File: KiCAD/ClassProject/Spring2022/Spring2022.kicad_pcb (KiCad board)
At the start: 2 copper layers, 211 x 39 mm, 40 parts, among them U1 FUB-MINI, U2 74HC595, U3 74HC595, U4 74HC595, U5 74HC595, U6 74HC595, U7 74HC595

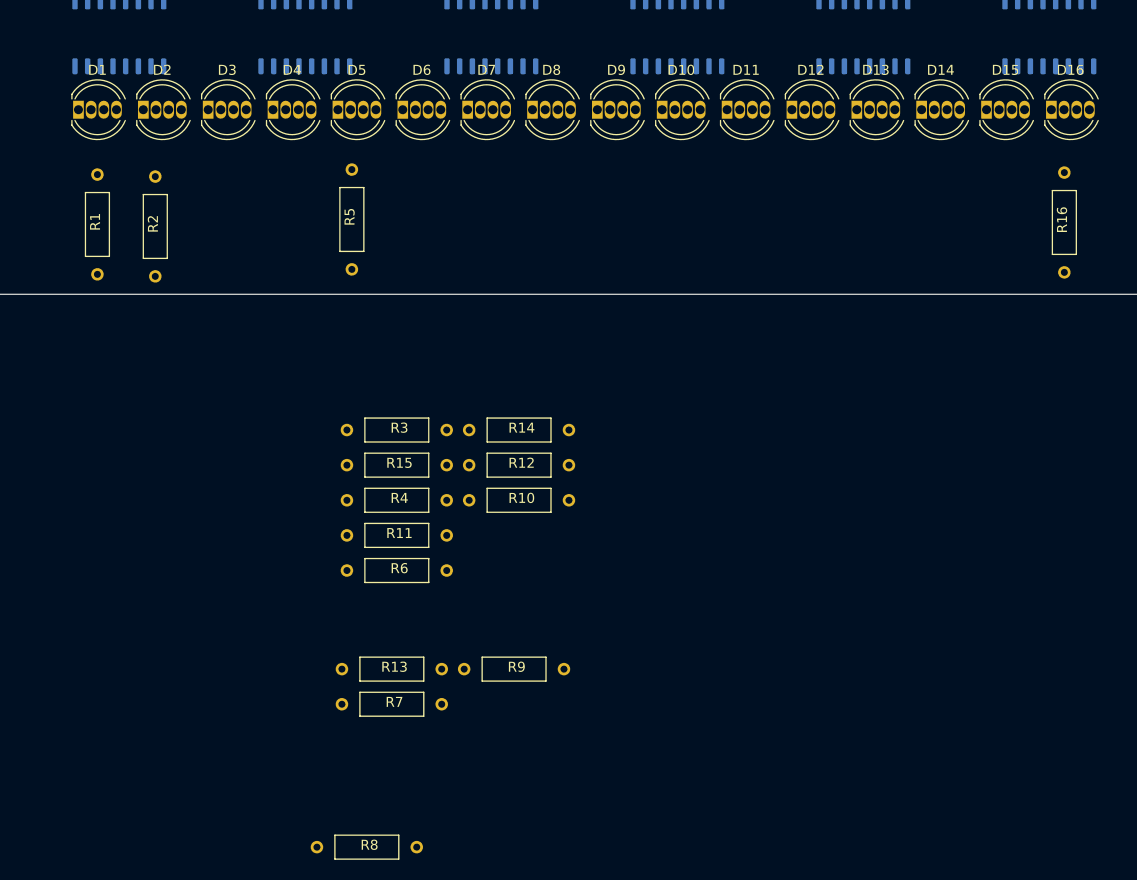
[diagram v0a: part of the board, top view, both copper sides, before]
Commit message: LED resistors update layout
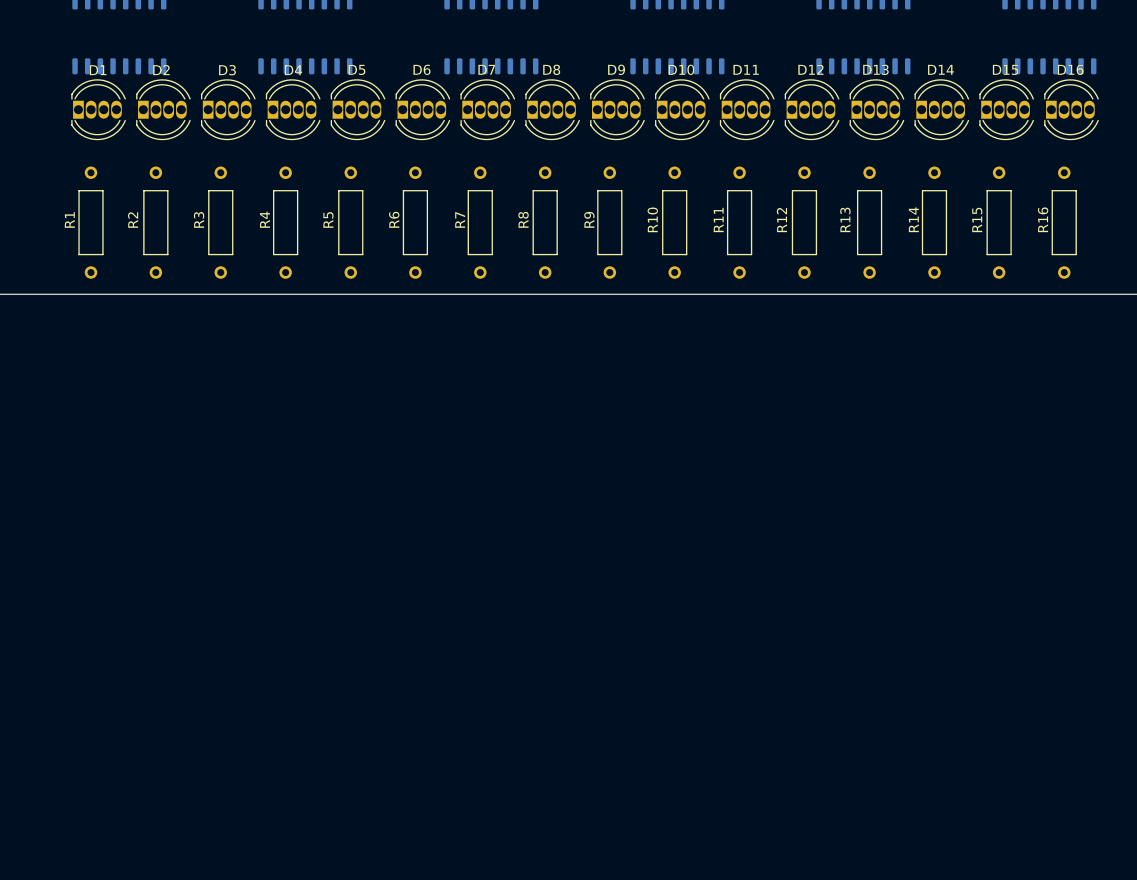
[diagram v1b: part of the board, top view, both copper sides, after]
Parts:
- moved R13 65.5 mm to (249.8, 51.8), turned to 90 degrees
- moved R8 65.1 mm to (217.3, 51.8), turned to 90 degrees
- moved R15 65.1 mm to (262.8, 51.8), turned to 90 degrees
- moved R7 49.1 mm to (210.8, 51.8), turned to 90 degrees
- moved R14 46.5 mm to (256.3, 51.8), turned to 90 degrees
- moved R11 46.5 mm to (236.8, 51.8), turned to 90 degrees
- moved R9 45.8 mm to (223.7, 51.8), turned to 90 degrees
- moved R12 37.5 mm to (243.3, 51.8), turned to 90 degrees
- moved R6 34.9 mm to (204.3, 51.8), turned to 90 degrees
- moved R10 31.9 mm to (230.3, 51.8), turned to 90 degrees
- moved R4 30.0 mm to (191.3, 51.8), turned to 90 degrees
- moved R3 27.3 mm to (184.8, 51.8), turned to 90 degrees
- moved R1 0.67 mm to (171.8, 51.8)
- moved R2 0.39 mm to (178.3, 51.8)
- moved R5 0.33 mm to (197.8, 51.8)

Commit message: Nearly finished schematic and routing.
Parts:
- added C1: PLP-000068, a_pontech:CAP-NON-POLAR-0603, B.Cu at (141.0, 50.0)
- added C2: PLP-000068, a_pontech:CAP-NON-POLAR-0603, B.Cu at (141.0, 51.7)
- added C3: PLP-000068, a_pontech:CAP-NON-POLAR-0603, B.Cu at (142.5, 40.5)
- added C4: PLP-000068, a_pontech:CAP-NON-POLAR-0603, B.Cu at (162.7, 40.9)
- added C5: PLP-000409, a_pontech:CAP-NON-POLAR-0603, B.Cu at (164.3, 40.9)
- added LED11: IRLED1503, 74_ClassProj_IRFootprint:IR1503, F.Cu at (154.3, 25.4)
- added R17: PLP-000270, a_pontech:R_0603_1608Metric, B.Cu at (145.5, 46.2)
- added R18: PLP-000270, a_pontech:R_0603_1608Metric, B.Cu at (145.0, 33.8)
- added R19: PLP-000031, a_pontech:R_0603_1608Metric, B.Cu at (154.4, 28.9)
- added R20: PLP-000091, a_pontech:R_0603_1608Metric, B.Cu at (155.2, 43.3)
- added R21: PLP-000091, a_pontech:R_0603_1608Metric, B.Cu at (155.2, 38.2)
- added R22: PLP-000091, a_pontech:R_0603_1608Metric, B.Cu at (155.2, 39.9)
- added R23: PLP-000091, a_pontech:R_0603_1608Metric, B.Cu at (155.2, 41.6)
- added R24: PLP-000091, a_pontech:R_0603_1608Metric, B.Cu at (149.8, 39.9)
- added R25: PLP-000091, a_pontech:R_0603_1608Metric, B.Cu at (149.8, 38.2)
- added R26: PLP-000091, a_pontech:R_0603_1608Metric, B.Cu at (149.8, 43.3)
- added R27: PLP-000029, a_pontech:R_0603_1608Metric, B.Cu at (149.8, 41.6)
- added R28: PLP-000029, a_pontech:R_0603_1608Metric, B.Cu at (160.5, 46.9)
- added R29: PLP-000029, a_pontech:R_0603_1608Metric, B.Cu at (160.5, 45.1)
- added U10: LM35-LP, 74_mehdi:TO-92L_Inline, F.Cu at (142.1, 54.5)
- added U11: SHT40-AD1B-R3, 74_eduardo_aaron:SHTC1Humidity_temp_footprint, B.Cu at (140.2, 40.5)
- added U12: LIS2DE12TR, 74_LIS2DE12TR:LIS2DE12TR, B.Cu at (159.3, 40.4)
- added U8: PLP-000201, a_pontech:PLP-000201, F.Cu at (141.5, 25.9)
- added U9: IS1871SF, 74_Kevin:Bluetooth_IC_IS1871SF-202-TRAY, B.Cu at (151.7, 54.7)
- moved R1 102.9 mm to (272.1, 28.8), turned to 270 degrees
- moved D1 102.8 mm to (273.3, 40.1), turned to 180 degrees
- moved R16 97.5 mm to (174.5, 28.8), turned to 270 degrees
- moved U2 95.8 mm to (269.2, 47.7), turned to 270 degrees
- moved U7 93.0 mm to (176.0, 47.7), turned to 270 degrees
- moved D16 92.2 mm to (175.8, 40.1), turned to 180 degrees
- moved R2 90.3 mm to (265.6, 28.8), turned to 270 degrees
- moved D2 89.8 mm to (266.8, 40.1), turned to 180 degrees
- moved R15 84.9 mm to (181.1, 28.8), turned to 270 degrees
- moved D15 79.2 mm to (182.3, 40.1), turned to 180 degrees
- moved R3 77.8 mm to (259.1, 28.8), turned to 270 degrees
- moved D3 76.8 mm to (260.3, 40.1), turned to 180 degrees
- moved R14 72.5 mm to (187.5, 28.8), turned to 270 degrees
- moved D14 66.2 mm to (188.8, 40.1), turned to 180 degrees
- moved R4 65.5 mm to (252.6, 28.8), turned to 270 degrees
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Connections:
- R1 pad 1: Net-(R1-Pad1) -> GND
- R10 pad 1: Net-(R1-Pad1) -> GND
- R11 pad 1: Net-(R1-Pad1) -> GND
- R12 pad 1: Net-(R1-Pad1) -> GND
- R13 pad 1: Net-(R1-Pad1) -> GND
- R14 pad 1: Net-(R1-Pad1) -> GND
- R15 pad 1: Net-(R1-Pad1) -> GND
- R16 pad 1: Net-(R1-Pad1) -> GND
- R2 pad 1: Net-(R1-Pad1) -> GND
- R3 pad 1: Net-(R1-Pad1) -> GND
- R4 pad 1: Net-(R1-Pad1) -> GND
- R5 pad 1: Net-(R1-Pad1) -> GND
- R6 pad 1: Net-(R1-Pad1) -> GND
- R7 pad 1: Net-(R1-Pad1) -> GND
- R8 pad 1: Net-(R1-Pad1) -> GND
- R9 pad 1: Net-(R1-Pad1) -> GND
- U1 pad 23: (no net) -> MISO
- U1 pad 29: (no net) -> I2C-SCK
- U1 pad 3: (no net) -> +3V3
- U1 pad 30: (no net) -> I2C-SDA
- U1 pad 38: (no net) -> +3V3
- U2 pad 10: +3V3 -> +4V
- U2 pad 16: +3V3 -> +4V
- U3 pad 10: +3V3 -> +4V
- U3 pad 16: (no net) -> +4V
- U4 pad 10: +3V3 -> +4V
- U4 pad 16: (no net) -> +4V
- U5 pad 10: +3V3 -> +4V
- U5 pad 16: (no net) -> +4V
- U6 pad 10: +3V3 -> +4V
- U6 pad 16: (no net) -> +4V
- U7 pad 10: +3V3 -> +4V
- U7 pad 16: (no net) -> +4V
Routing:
- net SCK: track 0.00 -> 159.6 mm, vias 0 -> 7
- net +4V: track 0.00 -> 146.0 mm, vias 0 -> 12
- net GND: track 0.00 -> 124.8 mm
- net DISPLAY-CLK: track 0.00 -> 124.6 mm, vias 0 -> 6
- net ~LED-OE: track 0.00 -> 120.1 mm, vias 0 -> 6
- net MOSI: track 0.00 -> 32.0 mm
- net Net-(U6-Pad14): track 0.00 -> 18.3 mm
- net Net-(U4-Pad14): track 0.00 -> 17.2 mm
- net Net-(U5-Pad14): track 0.00 -> 17.2 mm
- net Net-(U3-Pad14): track 0.00 -> 17.2 mm
- net Net-(U2-Pad14): track 0.00 -> 16.9 mm
- net Net-(D3-Pad3): track 0.00 -> 16.1 mm
- net +3V3: track 0.00 -> 15.4 mm
- net Net-(D6-Pad1): track 0.00 -> 14.4 mm
- net Net-(D8-Pad4): track 0.00 -> 13.4 mm
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- added copper zone on B.Cu, net GND
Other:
- net class Default: clearance 0.2 -> 0.1524; trace_width 0.25 -> 0.1524
- rule trace_clearance: 0.2 -> 0.1524
- rule trace_min: 0.2 -> 0.1524
- board text added: "10K"
- board text added: "I2C"
- board text added: "I2C-SCK"
- board text added: "I2C-SDA"
- board text added: "SPI"

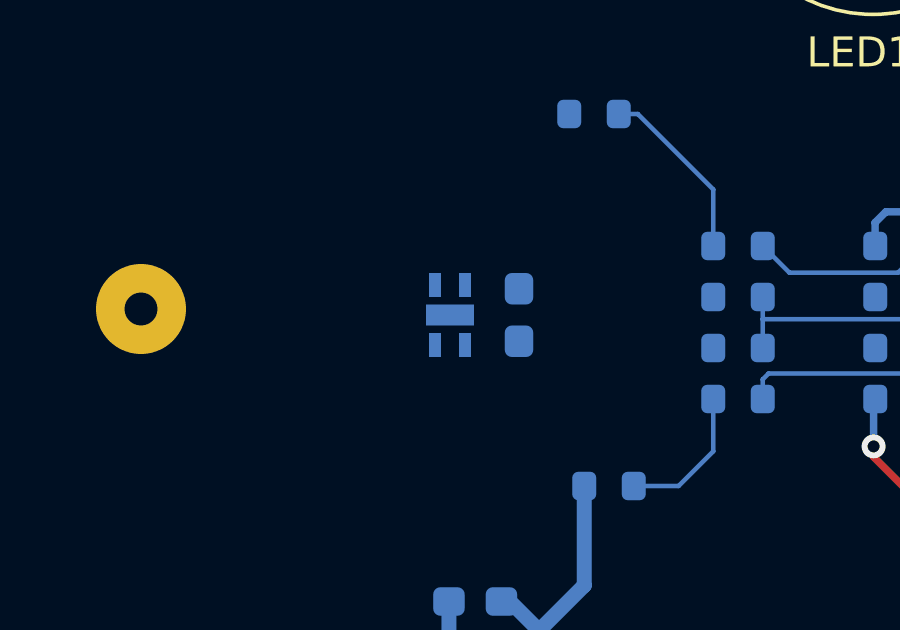
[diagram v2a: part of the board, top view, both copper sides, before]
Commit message: Re-Saved humidity sensor changes to close KiCad
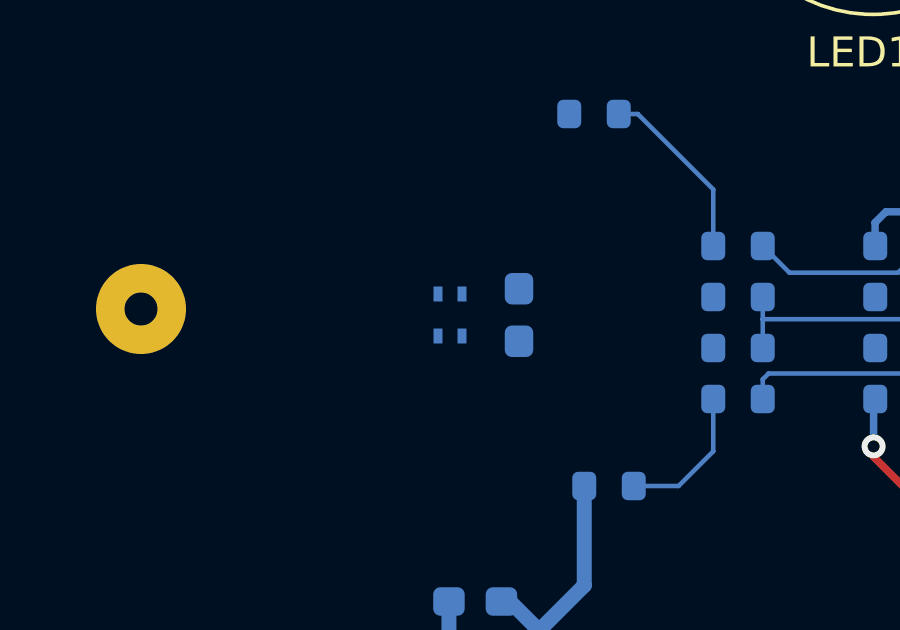
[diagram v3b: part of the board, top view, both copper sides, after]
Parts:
- U11: footprint 74_eduardo_aaron:SHTC1Humidity_temp_footprint -> 74_eduardo_aaron:SHT4X
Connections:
- LED11 pad 1: (no net) -> /IR TX/RX/IR-TX
- R23 pad 1: (no net) -> /Accelerometer/SPI-CS
- R24 pad 1: (no net) -> /Accelerometer/I2C-A0
- U1 pad 1: (no net) -> Net-(U1-Pad1)
- U1 pad 10: (no net) -> Net-(U1-Pad10)
- U1 pad 11: (no net) -> Net-(U1-Pad11)
- U1 pad 12: (no net) -> Net-(U1-Pad12)
- U1 pad 13: (no net) -> Net-(U1-Pad13)
- U1 pad 14: (no net) -> Net-(U1-Pad14)
- U1 pad 15: (no net) -> Net-(U1-Pad15)
- U1 pad 16: (no net) -> Net-(U1-Pad16)
- U1 pad 17: (no net) -> Net-(U1-Pad17)
- U1 pad 18: (no net) -> Net-(U1-Pad18)
- U1 pad 19: (no net) -> Net-(U1-Pad19)
- U1 pad 20: (no net) -> Net-(U1-Pad20)
- U1 pad 21: (no net) -> Net-(U1-Pad21)
- U1 pad 24: (no net) -> Net-(U1-Pad24)
- U1 pad 25: (no net) -> Net-(U1-Pad25)
- U1 pad 26: (no net) -> Net-(U1-Pad26)
- U1 pad 27: (no net) -> Net-(U1-Pad27)
- U1 pad 28: (no net) -> Net-(U1-Pad28)
- U1 pad 31: (no net) -> Net-(U1-Pad31)
- U1 pad 32: (no net) -> Net-(U1-Pad32)
- U1 pad 33: (no net) -> Net-(U1-Pad33)
- U1 pad 34: (no net) -> Net-(U1-Pad34)
- U1 pad 35: (no net) -> Net-(U1-Pad35)
- U1 pad 36: (no net) -> Net-(U1-Pad36)
- U1 pad 37: (no net) -> Net-(U1-Pad37)
- U1 pad 4: (no net) -> Net-(U1-Pad4)
- U1 pad 5: (no net) -> Net-(U1-Pad5)
- U1 pad 6: (no net) -> Net-(U1-Pad6)
- U1 pad 8: (no net) -> Net-(U1-Pad8)
- U1 pad 9: (no net) -> Net-(U1-Pad9)
- U11 pad 1: +3V3 -> I2C-SDA
- U11 pad 3: I2C-SDA -> +3V3
- U2 pad 9: (no net) -> Net-(U2-Pad9)
- U8 pad 3: (no net) -> /IR TX/RX/IR-RX
- U9 pad 1: (no net) -> Net-(U9-Pad1)
- U9 pad 10: (no net) -> Net-(U9-Pad10)
- U9 pad 11: (no net) -> Net-(U9-Pad11)
- U9 pad 12: (no net) -> Net-(U9-Pad12)
- U9 pad 13: (no net) -> Net-(U9-Pad13)
- U9 pad 14: (no net) -> Net-(U9-Pad14)
- U9 pad 15: (no net) -> Net-(U9-Pad15)
- U9 pad 16: (no net) -> Net-(U9-Pad16)
- U9 pad 17: (no net) -> Net-(U9-Pad17)
- U9 pad 18: (no net) -> Net-(U9-Pad18)
- U9 pad 19: (no net) -> Net-(U9-Pad19)
- U9 pad 2: (no net) -> Net-(U9-Pad2)
- U9 pad 20: (no net) -> Net-(U9-Pad20)
- U9 pad 21: (no net) -> Net-(U9-Pad21)
- U9 pad 22: (no net) -> Net-(U9-Pad22)
- U9 pad 23: (no net) -> Net-(U9-Pad23)
- U9 pad 24: (no net) -> Net-(U9-Pad24)
- U9 pad 25: (no net) -> Net-(U9-Pad25)
- U9 pad 26: (no net) -> Net-(U9-Pad26)
- U9 pad 27: (no net) -> Net-(U9-Pad27)
- U9 pad 28: (no net) -> Net-(U9-Pad28)
- U9 pad 29: (no net) -> Net-(U9-Pad29)
- U9 pad 3: (no net) -> Net-(U9-Pad3)
- U9 pad 30: (no net) -> Net-(U9-Pad30)
- U9 pad 31: (no net) -> Net-(U9-Pad31)
- U9 pad 32: (no net) -> Net-(U9-Pad32)
- U9 pad 4: (no net) -> Net-(U9-Pad4)
- U9 pad 5: (no net) -> Net-(U9-Pad5)
- U9 pad 6: (no net) -> Net-(U9-Pad6)
- U9 pad 7: (no net) -> Net-(U9-Pad7)
- U9 pad 8: (no net) -> Net-(U9-Pad8)
- U9 pad 9: (no net) -> Net-(U9-Pad9)
